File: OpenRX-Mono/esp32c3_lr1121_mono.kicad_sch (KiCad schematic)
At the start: 61 parts, among them J1 Conn_Coaxial_Small, T1 0900PC16J0042001E, U1 ESP32-C3, U2 TLV75533PDQNR, U3 LR1121IMLTRT, U4 RFX2401C, U5 SKY13373-460LF, X1 CJ17-400001010B20

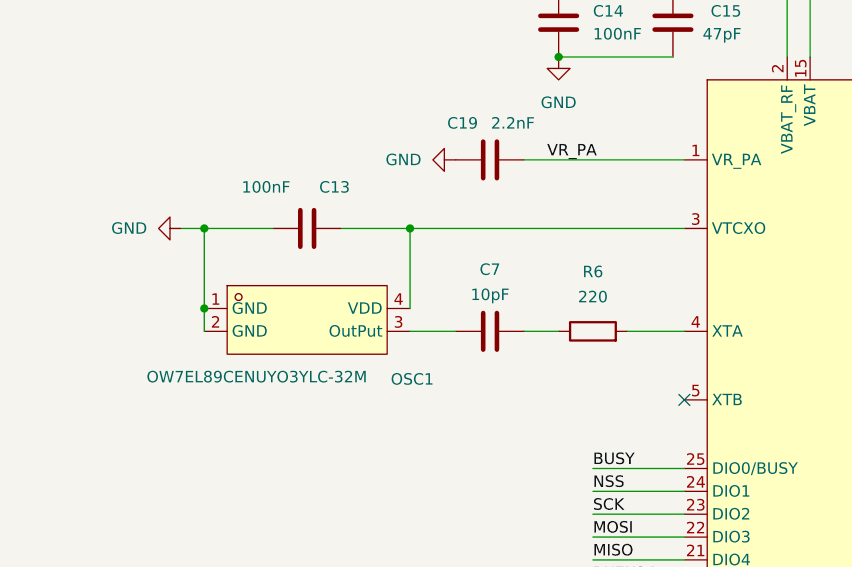
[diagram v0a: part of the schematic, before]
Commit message: changed 3.3V supply on clocks, added text, enlarged pads
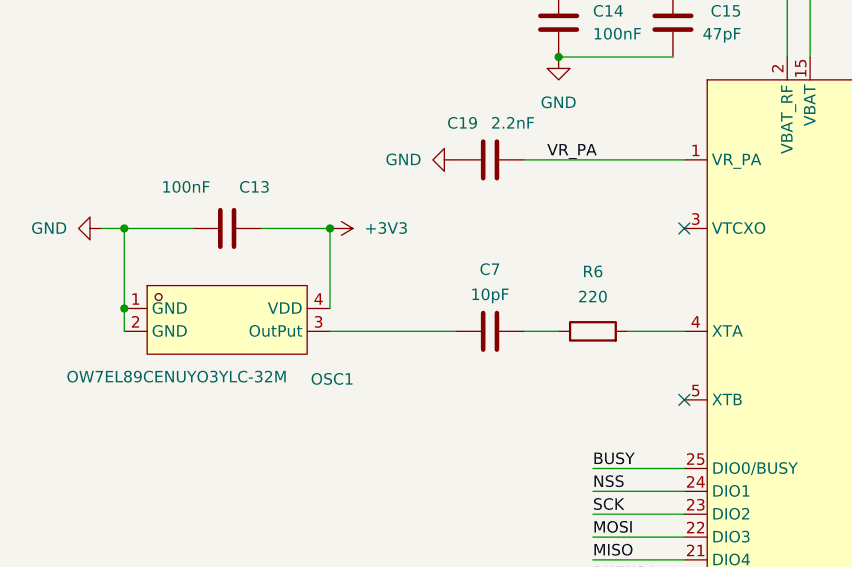
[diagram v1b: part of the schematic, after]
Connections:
- net +3V3: now also C13.2, OSC1.4 (VDD)
- now unconnected: U3.3 (VTCXO)
- no-connect marks 23 -> 24
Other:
- moved on the sheet: C13, OSC1
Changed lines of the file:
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@@
 	)
 	(junction
-		(at 58.42 182.88)
+		(at 49.53 182.88)
 		(diameter 0)
 		(color 0 0 0 0)
@@
 	)
 	(junction
+		(at 72.39 182.88)
+		(diameter 0)
+		(color 0 0 0 0)
+	)
+	(junction
 		(at 184.15 36.83)
 		(diameter 0)
@@
 	)
 	(junction
-		(at 81.28 182.88)
-		(diameter 0)
-		(color 0 0 0 0)
-	)
-	(junction
 		(at 243.84 78.74)
 		(diameter 0)
@@
 	)
 	(junction
-		(at 58.42 191.77)
+		(at 49.53 191.77)
 		(diameter 0)
 		(color 0 0 0 0)
@@
 	)
 	(no_connect
+		(at 111.76 182.88)
+	)
+	(no_connect
 		(at 242.57 190.5)
 	)
@@
 	(wire
 		(pts
-			(xy 111.76 182.88) (xy 81.28 182.88)
-		)
-		(stroke
-			(width 0)
-			(type default)
-		)
-	)
-	(wire
-		(pts
 			(xy 126.5687 57.15) (xy 121.92 57.15)
 		)
@@
 	(wire
 		(pts
-			(xy 66.04 182.88) (xy 58.42 182.88)
+			(xy 57.15 182.88) (xy 49.53 182.88)
 		)
 		(stroke
@@
 	(wire
 		(pts
-			(xy 58.42 182.88) (xy 58.42 191.77)
+			(xy 49.53 182.88) (xy 49.53 191.77)
 		)
 		(stroke
@@
 	(wire
 		(pts
-			(xy 81.28 182.88) (xy 81.28 191.77)
+			(xy 72.39 182.88) (xy 72.39 191.77)
 		)
 		(stroke
@@
 	(wire
 		(pts
-			(xy 58.42 191.77) (xy 58.42 194.31)
+			(xy 49.53 191.77) (xy 49.53 194.31)
 		)
 		(stroke
@@
 	(wire
 		(pts
-			(xy 73.66 182.88) (xy 81.28 182.88)
+			(xy 64.77 182.88) (xy 72.39 182.88)
 		)
 		(stroke
@@
 	(wire
 		(pts
-			(xy 81.28 194.31) (xy 86.36 194.31)
+			(xy 72.39 194.31) (xy 86.36 194.31)
 		)
 		(stroke
@@
 	(wire
 		(pts
-			(xy 55.88 182.88) (xy 58.42 182.88)
+			(xy 46.99 182.88) (xy 49.53 182.88)
 		)
 		(stroke
@@
 	(symbol
 		(lib_id "power:GND")
-		(at 55.88 182.88 270)
+		(at 46.99 182.88 270)
 		(unit 1)
 		(body_style 1)
@@
 		(fields_autoplaced yes)
 		(property "Reference" "#PWR010"
-			(at 49.53 182.88 0)
+			(at 40.64 182.88 0)
 			(hide yes)
 			(show_name no)
@@
 		)
 		(property "Value" "GND"
-			(at 52.07 182.8799 90)
+			(at 43.18 182.8799 90)
 			(show_name no)
 			(do_not_autoplace no)
@@
 		)
 		(property "Footprint" ""
-			(at 55.88 182.88 0)
+			(at 46.99 182.88 0)
 			(hide yes)
 			(show_name no)
@@
 		)
 		(property "Datasheet" ""
-			(at 55.88 182.88 0)
+			(at 46.99 182.88 0)
 			(hide yes)
 			(show_name no)
@@
 		)
 		(property "Description" "Power symbol creates a global label with name \"GND\" , ground"
-			(at 55.88 182.88 0)
+			(at 46.99 182.88 0)
 			(hide yes)
 			(show_name no)
@@
 	(symbol
 		(lib_id "OpenRX-Shared:OW7EL89CENUYO3YLC-32M")
-		(at 69.85 193.04 0)
+		(at 60.96 193.04 0)
 		(unit 1)
 		(body_style 1)
@@
 		(dnp no)
 		(property "Reference" "OSC1"
-			(at 81.534 199.644 0)
+			(at 72.644 199.644 0)
 			(show_name no)
 			(do_not_autoplace no)
@@
 		)
 		(property "Value" "OW7EL89CENUYO3YLC-32M"
-			(at 64.262 199.39 0)
+			(at 55.372 199.39 0)
 			(show_name no)
 			(do_not_autoplace no)
@@
 		)
 		(property "Footprint" "OpenRX-Shared:OSC-SMD_4P-L2.0-W1.6-BL_TXC_7Z"
-			(at 69.85 201.93 0)
+			(at 60.96 201.93 0)
 			(hide yes)
 			(show_name no)
@@
 		)
 		(property "Datasheet" ""
-			(at 69.85 193.04 0)
+			(at 60.96 193.04 0)
 			(hide yes)
 			(show_name no)
@@
 		)
 		(property "Description" ""
-			(at 69.85 193.04 0)
+			(at 60.96 193.04 0)
 			(hide yes)
 			(show_name no)
@@
 		)
 		(property "LCSC Part" "C22381772"
-			(at 69.85 204.47 0)
+			(at 60.96 204.47 0)
 			(hide yes)
 			(show_name no)
@@
 	)
 	(symbol
+		(lib_id "power:+3V3")
+		(at 72.39 182.88 270)
+		(unit 1)
+		(body_style 1)
+		(exclude_from_sim no)
+		(in_bom yes)
+		(on_board yes)
+		(in_pos_files yes)
+		(dnp no)
+		(fields_autoplaced yes)
+		(property "Reference" "#PWR038"
+			(at 68.58 182.88 0)
+			(hide yes)
+			(show_name no)
+			(do_not_autoplace no)
+			(effects
+				(font
+					(size 1.27 1.27)
+				)
+			)
+		)
+		(property "Value" "+3V3"
+			(at 76.2 182.8799 90)
+			(show_name no)
+			(do_not_autoplace no)
+			(effects
+				(font
+					(size 1.27 1.27)
+				)
+				(justify left)
+			)
+		)
+		(property "Footprint" ""
+			(at 72.39 182.88 0)
+			(hide yes)
+			(show_name no)
+			(do_not_autoplace no)
+			(effects
+				(font
+					(size 1.27 1.27)
+				)
+			)
+		)
+		(property "Datasheet" ""
+			(at 72.39 182.88 0)
+			(hide yes)
+			(show_name no)
+			(do_not_autoplace no)
+			(effects
+				(font
+					(size 1.27 1.27)
+				)
+			)
+		)
+		(property "Description" "Power symbol creates a global label with name \"+3V3\""
+			(at 72.39 182.88 0)
+			(hide yes)
+			(show_name no)
+			(do_not_autoplace no)
+			(effects
+				(font
+					(size 1.27 1.27)
+				)
+			)
+		)
+		(pin "1"
+		)
+		(instances
+			(project "OpenRX-Mono"
+				(path "/b1c2d3e4-f5a6-7890-bcde-f12345678901/f1e2d3c4-b5a6-7890-1234-567890fedcba"
+					(reference "#PWR038")
+					(unit 1)
+				)
+			)
+		)
+	)
+	(symbol
 		(lib_id "power:GND")
 		(at 212.09 212.09 0)
@@
 	(symbol
 		(lib_id "Device:C")
-		(at 69.85 182.88 90)
+		(at 60.96 182.88 90)
 		(mirror x)
 		(unit 1)
@@
 		(dnp no)
 		(property "Reference" "C13"
-			(at 72.898 178.308 90)
+			(at 64.008 178.308 90)
 			(show_name no)
 			(do_not_autoplace no)
@@
 		)
 		(property "Value" "100nF"
-			(at 65.278 178.308 90)
+			(at 56.388 178.308 90)
 			(show_name no)
 			(do_not_autoplace no)
@@
 		)
 		(property "Footprint" "Capacitor_SMD:C_0201_0603Metric"
-			(at 73.66 183.8452 0)
+			(at 64.77 183.8452 0)
 			(hide yes)
 			(show_name no)
@@
 		)
 		(property "Datasheet" ""
-			(at 69.85 182.88 0)
+			(at 60.96 182.88 0)
 			(hide yes)
 			(show_name no)
@@
 		)
 		(property "Description" "Unpolarized capacitor"
-			(at 69.85 182.88 0)
+			(at 60.96 182.88 0)
 			(hide yes)
 			(show_name no)
@@
 		)
 		(property "LCSC" "C76939"
-			(at 36.83 25.4 0)
+			(at 27.94 25.4 0)
 			(hide yes)
 			(show_name no)
@@
 		)
 		(property "LCSC Part" "C76939"
-			(at 36.83 25.4 0)
+			(at 27.94 25.4 0)
 			(hide yes)
 			(show_name no)
